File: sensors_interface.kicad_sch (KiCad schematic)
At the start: 16 parts, among them J10 SP13 Socket, J4 Conn_01x08_Socket, J5 Conn_01x08_Socket, J9 SP13 Socket, Q2 DMP2240UDM-7, U4 MT3608

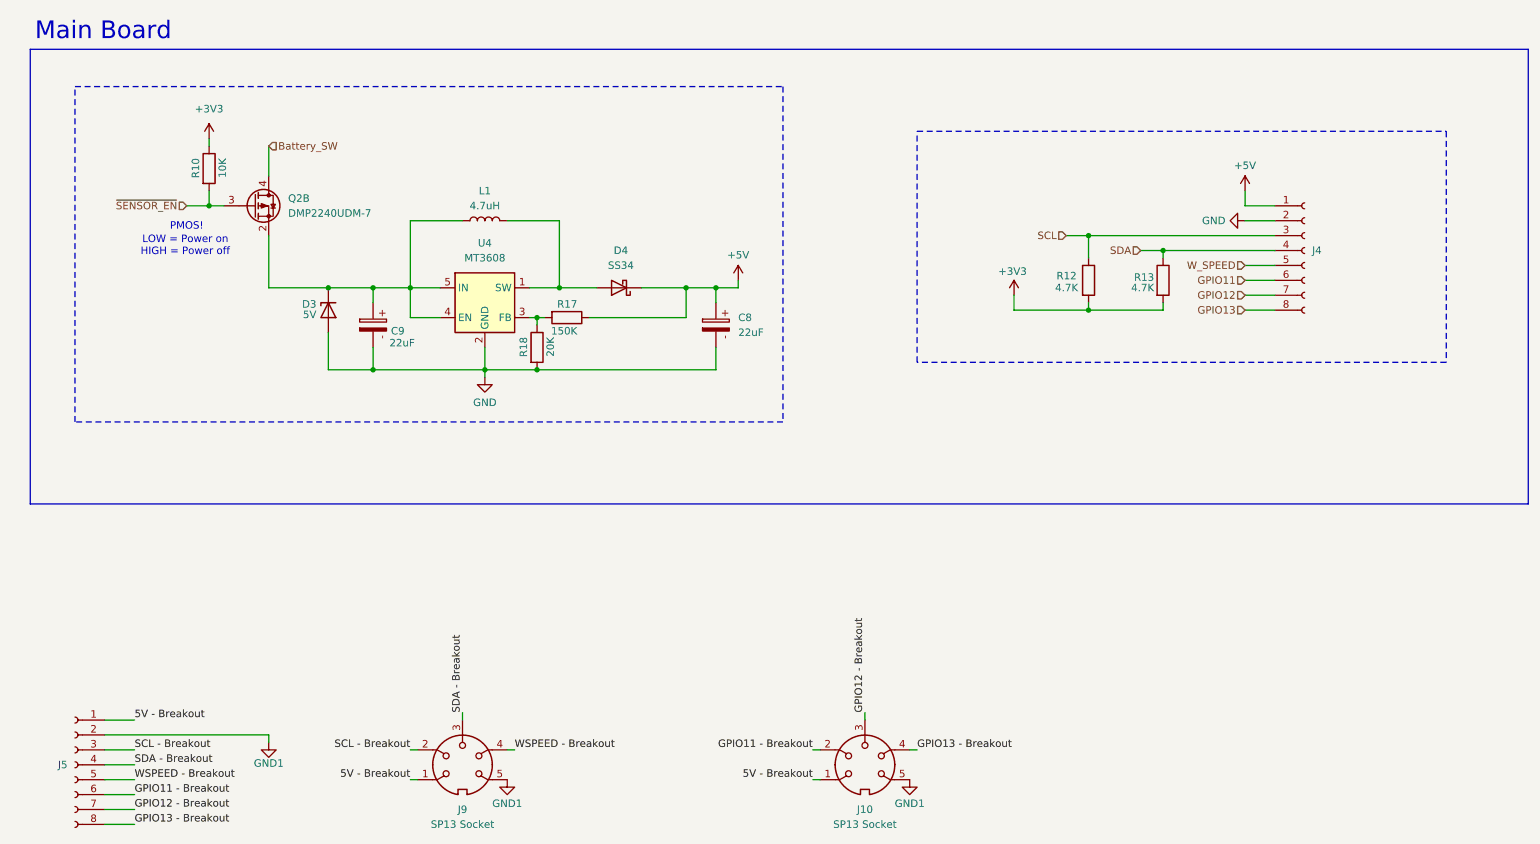
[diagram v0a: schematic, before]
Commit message: - Chnaged to USBLC6-2SC6 for USB ESD protection - Expose 5V rail to Breakout - Fixed missing battery track to power sensors;
- TO DO: open collector mosfet driver to 5V reg
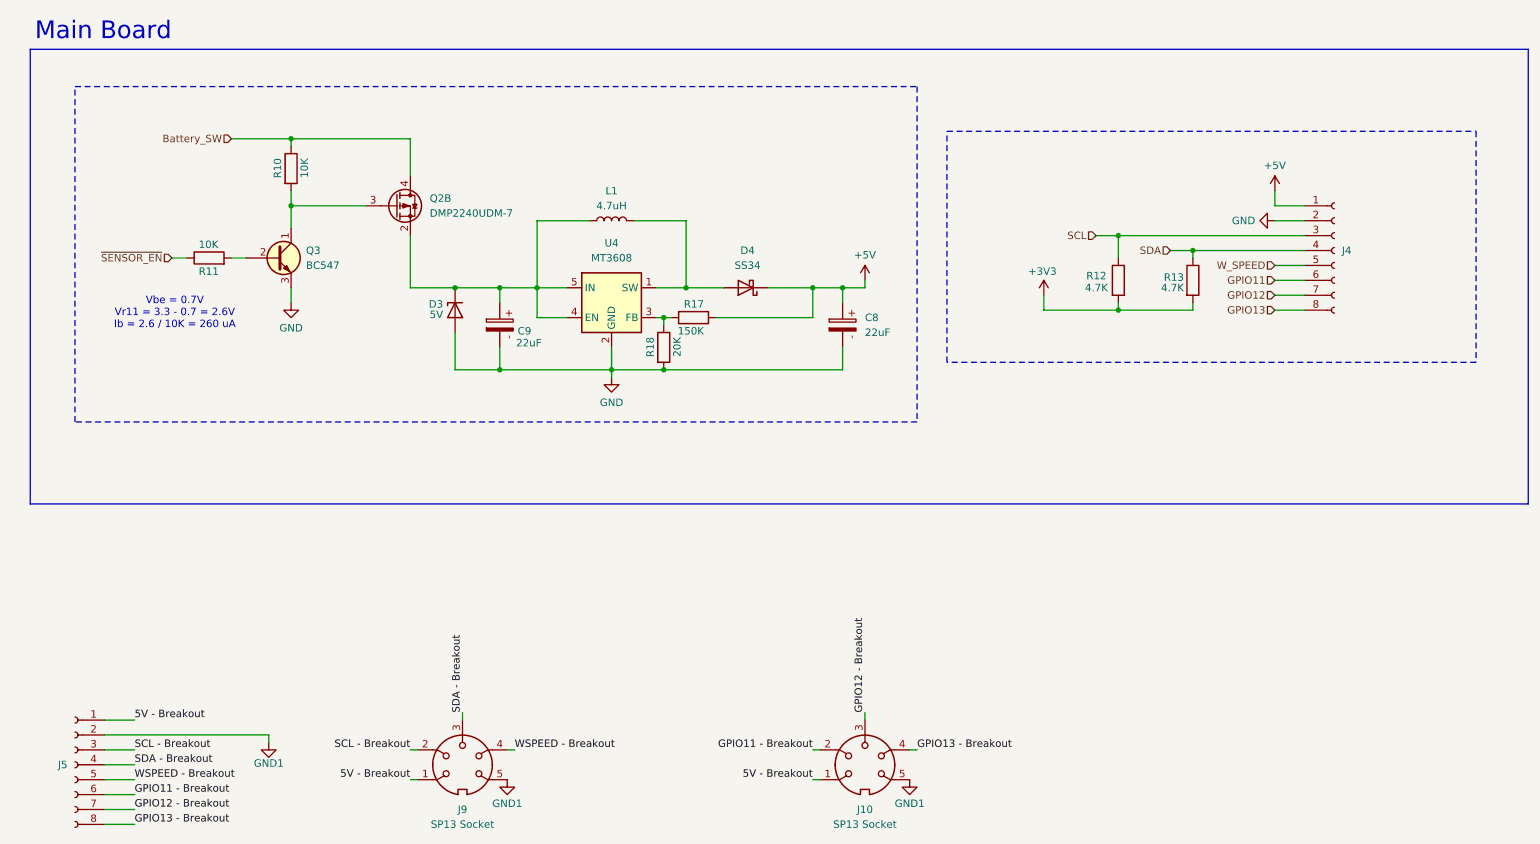
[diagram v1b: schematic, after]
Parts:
- added Q3: BC547, PCM_Package_TO_SOT_THT_AKL:TO-92_Inline_Wide_CBE, symbol PCM_Transistor_BJT_AKL:BC547
- added R11: 10K, Resistor_SMD:R_1206_3216Metric, symbol Device:R
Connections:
- net +3V3: no longer R10.1
- net Battery_SW: now also R10.1
- net GND: now also Q3.3 (E)
- net ~{SENSOR_EN}: now also R11.1; no longer Q2.3 (G), R10.2
- new net: Q2.3 (G), Q3.1 (C), R10.2
- new net: Q3.2 (B), R11.2
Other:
- note added: "Vbe = 0.7V Vr11 = 3.3 - 0.7 = 2.6V Ib = 2.6 / 10K = 260 uA"
- note removed: "LOW = Power on HIGH = Power off"
- note removed: "PMOS!"
- moved on the sheet: C8, C9, D3, D4, J4, L1, Q2B, R10, R12, R13, R17, R18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

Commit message: - Connected open collector mosfet driver to 5V reg - Re-routed tracks related to NMOS
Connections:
- net ~{SENSOR_EN} renamed SENSOR_EN
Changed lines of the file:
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@@
+	)
+	(junction
+		(at 87.63 57.15)
+		(diameter 0)
+		(color 0 0 0 0)
 	)
 	(junction
@@
 	(wire
 		(pts
+			(xy 87.63 57.15) (xy 87.63 63.5)
+		)
+		(stroke
+			(width 0)
+			(type default)
+		)
+	)
+	(wire
+		(pts
 			(xy 35.56 139.7) (xy 63.5 139.7)
 		)
@@
 	(wire
 		(pts
-			(xy 87.63 54.61) (xy 87.63 63.5)
+			(xy 87.63 54.61) (xy 87.63 57.15)
 		)
 		(stroke
@@
 		)
 	)
-	(hierarchical_label "~{SENSOR_EN}"
+	(hierarchical_label "SENSOR_EN"
 		(shape input)
 		(at 46.99 58.42 180)
@@
 					(unit 1)
 				)
+			)
+		)
+	)
+	(symbol
+		(lib_id "power:PWR_FLAG")
+		(at 87.63 57.15 270)
+		(unit 1)
+		(body_style 1)
+		(exclude_from_sim no)
+		(in_bom yes)
+		(on_board yes)
+		(in_pos_files yes)
+		(dnp no)
+		(fields_autoplaced yes)
+		(property "Reference" "#FLG05"
+			(at 89.535 57.15 0)
+			(hide yes)
+			(show_name no)
+			(do_not_autoplace no)
+			(effects
+				(font
+					(size 1.27 1.27)
+				)
+			)
+		)
+		(property "Value" "PWR_FLAG"
+			(at 91.44 57.1499 90)
+			(show_name no)
+			(do_not_autoplace no)
+			(effects
+				(font
+					(size 1.27 1.27)
+				)
+				(justify left)
+			)
+		)
+		(property "Footprint" ""
+			(at 87.63 57.15 0)
+			(hide yes)
+			(show_name no)
+			(do_not_autoplace no)
+			(effects
+				(font
+					(size 1.27 1.27)
+				)
+			)
+		)
+		(property "Datasheet" ""
+			(at 87.63 57.15 0)
+			(hide yes)
+			(show_name no)
+			(do_not_autoplace no)
+			(effects
+				(font
+					(size 1.27 1.27)
+				)
+			)
+		)
+		(property "Description" "Special symbol for telling ERC where power comes from"
+			(at 87.63 57.15 0)
+			(hide yes)
+			(show_name no)
+			(do_not_autoplace no)
+			(effects
+				(font
+					(size 1.27 1.27)
+				)
+			)
+		)
+		(pin "1"
+		)
+		(instances
+			(project "Weather Station V2"
+				(path "/817e54af-ab8f-4cfe-9b63-ceac8d6d2a44/10b65a9a-b824-4f45-92b4-b4e156b1f43c"
+					(reference "#FLG05")
+					(unit 1)
+				)

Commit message: - Localized Libraries
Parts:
- C8, C9: footprint Capacitor_THT:CP_Radial_D4.0mm_P1.50mm -> FootprintsLib:CP_Radial_D4.0mm_P1.50mm; symbol PCM_SL_Capacitors:22uF_16V -> SymbolsLib:22uF_16V
- D3: footprint Diode_THT:D_DO-41_SOD81_P10.16mm_Horizontal -> FootprintsLib:D_DO-41_SOD81_P10.16mm_Horizontal; symbol Diode:1N47xxA -> SymbolsLib:1N47xxA
- D4: footprint Diode_SMD:D_SMA -> FootprintsLib:D_SMA; symbol Diode:SS34 -> SymbolsLib:SS34
- J10, J9: footprint SP13_5pin_holes:SP13_5pin_holes -> FootprintsLib:SP13_5pin_holes; symbol Connector:DIN-5 -> SymbolsLib:DIN-5
- J4, J5: footprint Connector_Hirose:Hirose_DF13-08P-1.25DSA_1x08_P1.25mm_Vertical -> FootprintsLib:Hirose_DF13-08P-1.25DSA_1x08_P1.25mm_Vertical; symbol Connector:Conn_01x08_Socket -> SymbolsLib:Conn_01x08_Socket
- L1: footprint Inductor_SMD:L_APV_APH0420 -> FootprintsLib:L_APV_APH0420; symbol Device:L -> SymbolsLib:L
- Q2: footprint Package_TO_SOT_SMD:SOT-23-6_Handsoldering -> FootprintsLib:SOT-23-6_Handsoldering; symbol Transistor_FET:Q_Dual_PMOS_G1S2G2D2S1D1 -> SymbolsLib:Q_Dual_PMOS_G1S2G2D2S1D1
- Q3: footprint PCM_Package_TO_SOT_THT_AKL:TO-92_Inline_Wide_CBE -> FootprintsLib:TO-92_Inline_Wide_CBE; symbol PCM_Transistor_BJT_AKL:BC547 -> SymbolsLib:BC547
- R10, R11, R12, R13, R17, R18: footprint Resistor_SMD:R_1206_3216Metric -> FootprintsLib:R_1206_3216Metric; symbol Device:R -> SymbolsLib:R
- U4: footprint Package_TO_SOT_SMD:SOT-23-6 -> FootprintsLib:SOT-23-6; symbol Regulator_Switching:MT3608 -> SymbolsLib:MT3608
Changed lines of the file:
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@@
 	)
 	(symbol
-		(lib_id "Regulator_Switching:MT3608")
+		(lib_id "SymbolsLib:MT3608")
 		(at 121.92 66.04 0)
 		(unit 1)
@@
 			)
 		)
-		(property "Footprint" "Package_TO_SOT_SMD:SOT-23-6"
+		(property "Footprint" "FootprintsLib:SOT-23-6"
 			(at 123.19 72.39 0)
 			(hide yes)
@@
 			)
 		)
-		(property "Datasheet" "https://www.olimex.com/Products/Breadboarding/BB-PWR-3608/resources/MT3608.pdf"
+		(property "Datasheet" "${KIPRJMOD}/Data_Sheets/MT3608.pdf"
 			(at 115.57 54.61 0)
 			(hide yes)
@@
 	)
 	(symbol
-		(lib_id "Connector:Conn_01x08_Socket")
+		(lib_id "SymbolsLib:Conn_01x08_Socket")
 		(at 245.11 57.15 0)
 		(unit 1)
@@
 			)
 		)
-		(property "Footprint" "Connector_Hirose:Hirose_DF13-08P-1.25DSA_1x08_P1.25mm_Vertical"
+		(property "Footprint" "FootprintsLib:Hirose_DF13-08P-1.25DSA_1x08_P1.25mm_Vertical"
 			(at 245.11 57.15 0)
 			(hide yes)
@@
 	)
 	(symbol
-		(lib_id "Transistor_FET:Q_Dual_PMOS_G1S2G2D2S1D1")
+		(lib_id "SymbolsLib:Q_Dual_PMOS_G1S2G2D2S1D1")
 		(at 85.09 49.53 0)
 		(unit 2)
@@
 			)
 		)
-		(property "Footprint" "Package_TO_SOT_SMD:SOT-23-6_Handsoldering"
+		(property "Footprint" "FootprintsLib:SOT-23-6_Handsoldering"
 			(at 86.36 49.53 0)
 			(hide yes)
@@
 	)
 	(symbol
-		(lib_id "Connector:DIN-5")
+		(lib_id "SymbolsLib:DIN-5")
 		(at 96.52 144.78 0)
 		(unit 1)
@@
 			)
 		)
-		(property "Footprint" "SP13_5pin_holes:SP13_5pin_holes"
+		(property "Footprint" "FootprintsLib:SP13_5pin_holes"
 			(at 96.52 144.78 0)
 			(hide yes)
@@
 			)
 		)
-		(property "Datasheet" "http://www.mouser.com/ds/2/18/40_c091_abd_e-75918.pdf"
+		(property "Datasheet" "${KIPRJMOD}/Data_Sheets/40_c091_abd_e-75918.pdf"
 			(at 96.52 144.78 0)
 			(hide yes)
@@
 	)
 	(symbol
-		(lib_id "PCM_Transistor_BJT_AKL:BC547")
+		(lib_id "SymbolsLib:BC547")
 		(at 64.77 58.42 0)
 		(unit 1)
@@
 			)
 		)
-		(property "Footprint" "PCM_Package_TO_SOT_THT_AKL:TO-92_Inline_Wide_CBE"
+		(property "Footprint" "FootprintsLib:TO-92_Inline_Wide_CBE"
 			(at 69.85 55.88 0)
 			(hide yes)
@@
 			)
 		)
-		(property "Datasheet" "https://www.tme.eu/Document/6c5d898a533a0762c2bc33eb26c283a8/BC546-550-DTE.pdf"
+		(property "Datasheet" "${KIPRJMOD}/Data_Sheets/BC546-550-DTE.pdf"
 			(at 64.77 58.42 0)
 			(hide yes)
@@
 	)
 	(symbol
-		(lib_id "Diode:1N47xxA")
+		(lib_id "SymbolsLib:1N47xxA")
 		(at 95.25 67.31 90)
 		(mirror x)
@@
 			)
 		)
-		(property "Footprint" "Diode_THT:D_DO-41_SOD81_P10.16mm_Horizontal"
+		(property "Footprint" "FootprintsLib:D_DO-41_SOD81_P10.16mm_Horizontal"
 			(at 99.695 67.31 0)
 			(hide yes)
@@
 			)
 		)
-		(property "Datasheet" "https://www.vishay.com/docs/85816/1n4728a.pdf"
+		(property "Datasheet" "${KIPRJMOD}/Data_Sheets/1n4728a.pdf"
 			(at 95.25 67.31 0)
 			(hide yes)
@@
 	)
 	(symbol
-		(lib_id "Connector:DIN-5")
+		(lib_id "SymbolsLib:DIN-5")
 		(at 165.1 144.78 0)
 		(unit 1)
@@
 			)
 		)
-		(property "Footprint" "SP13_5pin_holes:SP13_5pin_holes"
+		(property "Footprint" "FootprintsLib:SP13_5pin_holes"
 			(at 165.1 144.78 0)
 			(hide yes)
@@
 			)
 		)
-		(property "Datasheet" "http://www.mouser.com/ds/2/18/40_c091_abd_e-75918.pdf"
+		(property "Datasheet" "${KIPRJMOD}/Data_Sheets/40_c091_abd_e-75918.pdf"
 			(at 165.1 144.78 0)
 			(hide yes)
@@
 	)
 	(symbol
-		(lib_id "Device:R")
+		(lib_id "SymbolsLib:R")
 		(at 67.31 43.18 0)
 		(unit 1)
@@
 			)
 		)
-		(property "Footprint" "Resistor_SMD:R_1206_3216Metric"
+		(property "Footprint" "FootprintsLib:R_1206_3216Metric"
 			(at 65.532 43.18 90)
 			(hide yes)
@@
 	)
 	(symbol
-		(lib_id "Device:R")
+		(lib_id "SymbolsLib:R")
 		(at 53.34 58.42 90)
 		(unit 1)
@@
 			)
 		)
-		(property "Footprint" "Resistor_SMD:R_1206_3216Metric"
+		(property "Footprint" "FootprintsLib:R_1206_3216Metric"
 			(at 53.34 60.198 90)
 			(hide yes)
@@
 	)
 	(symbol
-		(lib_id "Device:R")
+		(lib_id "SymbolsLib:R")
 		(at 135.89 68.58 270)
 		(unit 1)
@@
 			)
 		)
-		(property "Footprint" "Resistor_SMD:R_1206_3216Metric"
+		(property "Footprint" "FootprintsLib:R_1206_3216Metric"
 			(at 135.89 66.802 90)
 			(hide yes)
@@
 	)
 	(symbol
-		(lib_id "Diode:SS34")
+		(lib_id "SymbolsLib:SS34")
 		(at 144.78 63.5 180)
 		(unit 1)
@@
 			)
 		)
-		(property "Footprint" "Diode_SMD:D_SMA"
+		(property "Footprint" "FootprintsLib:D_SMA"
 			(at 144.78 59.055 0)
 			(hide yes)
@@
 			)
 		)
-		(property "Datasheet" "https://www.vishay.com/docs/88751/ss32.pdf"
+		(property "Datasheet" "${KIPRJMOD}/Data_Sheets/ss32.pdf"
 			(at 144.78 63.5 0)
 			(hide yes)
@@
 	)
 	(symbol
-		(lib_id "Device:L")
+		(lib_id "SymbolsLib:L")
 		(at 121.92 52.07 90)
 		(unit 1)
@@
 			)
 		)
-		(property "Footprint" "Inductor_SMD:L_APV_APH0420"
+		(property "Footprint" "FootprintsLib:L_APV_APH0420"
 			(at 121.92 52.07 0)
 			(hide yes)
@@
 	)
 	(symbol
-		(lib_id "PCM_SL_Capacitors:22uF_16V")
+		(lib_id "SymbolsLib:22uF_16V")
 		(at 102.87 69.85 270)
 		(unit 1)
@@
 			)
 		)
-		(property "Footprint" "Capacitor_THT:CP_Radial_D4.0mm_P1.50mm"
+		(property "Footprint" "FootprintsLib:CP_Radial_D4.0mm_P1.50mm"
 			(at 99.06 70.612 0)
 			(hide yes)
@@
 	)
 	(symbol
-		(lib_id "Device:R")
+		(lib_id "SymbolsLib:R")
 		(at 130.81 73.66 0)
 		(unit 1)
@@
 			)
 		)
-		(property "Footprint" "Resistor_SMD:R_1206_3216Metric"
+		(property "Footprint" "FootprintsLib:R_1206_3216Metric"
 			(at 129.032 73.66 90)
 			(hide yes)
@@
 	)
 	(symbol
-		(lib_id "Connector:Conn_01x08_Socket")
+		(lib_id "SymbolsLib:Conn_01x08_Socket")
 		(at 30.48 144.78 0)
 		(mirror y)
@@
 			)
 		)
-		(property "Footprint" "Connector_Hirose:Hirose_DF13-08P-1.25DSA_1x08_P1.25mm_Vertical"
+		(property "Footprint" "FootprintsLib:Hirose_DF13-08P-1.25DSA_1x08_P1.25mm_Vertical"
 			(at 30.48 144.78 0)
 			(hide yes)
@@
 	)
 	(symbol
-		(lib_id "PCM_SL_Capacitors:22uF_16V")
+		(lib_id "SymbolsLib:22uF_16V")
 		(at 161.29 69.85 270)
 		(unit 1)
@@
 			)
 		)
-		(property "Footprint" "Capacitor_THT:CP_Radial_D4.0mm_P1.50mm"
+		(property "Footprint" "FootprintsLib:CP_Radial_D4.0mm_P1.50mm"
 			(at 157.48 70.612 0)
 			(hide yes)
@@
 	)
 	(symbol
-		(lib_id "Device:R")
+		(lib_id "SymbolsLib:R")
 		(at 208.28 62.23 0)
 		(unit 1)
@@
 			)
 		)
-		(property "Footprint" "Resistor_SMD:R_1206_3216Metric"
+		(property "Footprint" "FootprintsLib:R_1206_3216Metric"
 			(at 206.502 62.23 90)
 			(hide yes)
@@
 	)
 	(symbol
-		(lib_id "Device:R")
+		(lib_id "SymbolsLib:R")
 		(at 220.98 62.23 0)
 		(unit 1)
@@
 			)
 		)
-		(property "Footprint" "Resistor_SMD:R_1206_3216Metric"
+		(property "Footprint" "FootprintsLib:R_1206_3216Metric"
 			(at 219.202 62.23 90)
 			(hide yes)
